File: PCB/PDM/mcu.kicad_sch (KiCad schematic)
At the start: 31 parts, among them IC1 STM32L496ZGT6, IC2 AT25SF128A-SHB-T, Y1 48Mhz, Y2 32KHz

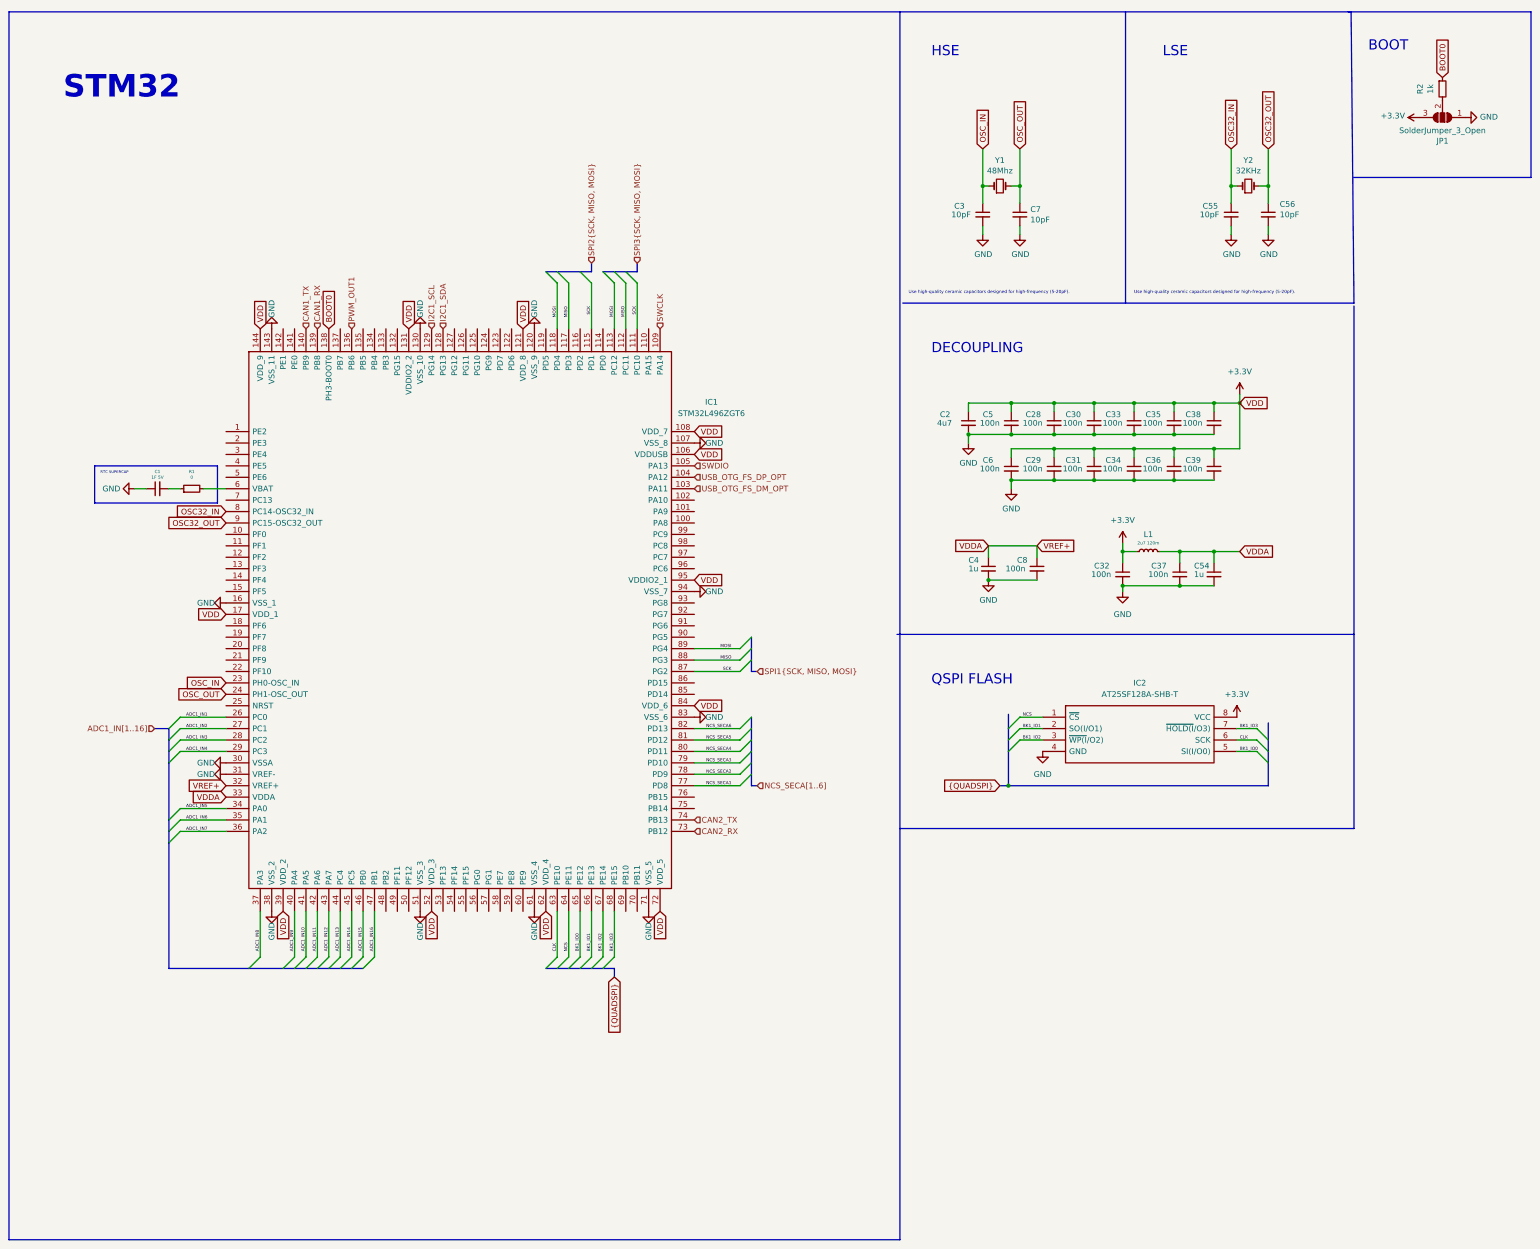
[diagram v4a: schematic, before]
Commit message: Finished high side section & fixed some ERC's errors
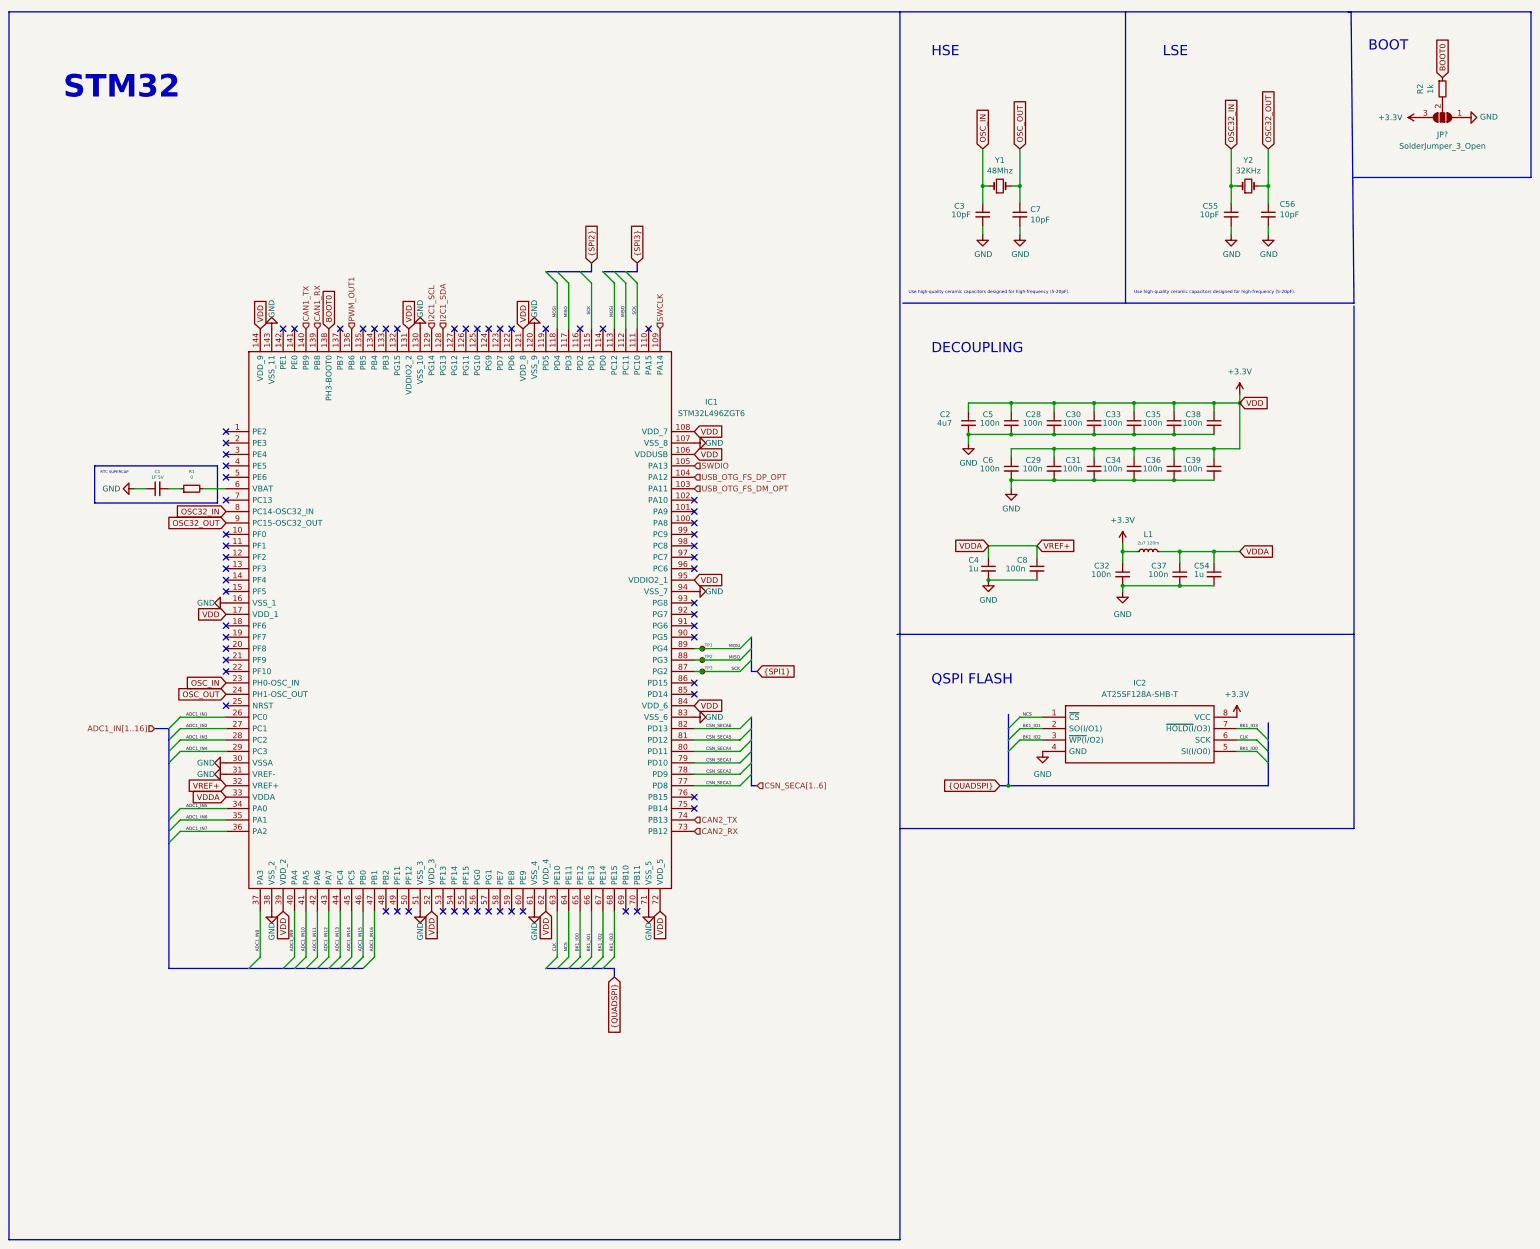
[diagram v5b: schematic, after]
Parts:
- removed JP1: SolderJumper_3_Open, Jumper:SolderJumper-3_P1.3mm_Open_RoundedPad1.0x1.5mm, symbol can2usb-rescue:SolderJumper_3_Open-Jumper
- added JP?: SolderJumper_3_Open, symbol Jumper:SolderJumper_3_Open
- added TP1, TP2, TP3: SPI1_TP, symbol Connector:TestPoint_Small
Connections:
- net +3.3V: now also JP?.3 (B)
- net GND: now also JP?.1 (A)
- net MISO: now also TP2.1
- net MOSI: now also TP1.1
- net SCK: now also TP3.1
- net at R2.2: now also JP?.2 (C)
- net NCS_SECA1 renamed CSN_SECA1
- net NCS_SECA2 renamed CSN_SECA2
- net NCS_SECA3 renamed CSN_SECA3
- net NCS_SECA4 renamed CSN_SECA4
- net NCS_SECA5 renamed CSN_SECA5
- net NCS_SECA6 renamed CSN_SECA6
- no-connect marks 0 -> 63

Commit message: Minor changes in HS sechmatics
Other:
- note added: "ADD adc protection"
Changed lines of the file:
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@@
   (bus_alias "QUADSPI" (members "CLK" "NCS" "BK1_IO0" "BK1_IO1" "BK1_IO2" "BK1_IO3"))
   (bus_alias "SPI1" (members "SCK" "MISO" "MOSI"))
+  (bus_alias "SPI3" (members "SCK" "MISO" "MOSI"))
   (bus_alias "SPI2" (members "SCK" "MISO" "MOSI"))
-  (bus_alias "SPI3" (members "SCK" "MISO" "MOSI"))
   (junction (at 279.4 109.22) (diameter 0) (color 0 0 0 0)
   )
@@
     (stroke (width 0) (type default) (color 0 0 0 0))
   )
-  (polyline (pts (xy 210.185 76.835) (xy 310.515 76.835))
+  (polyline (pts (xy 210.185 76.835) (xy 309.88 76.2))
     (stroke (width 0) (type default) (color 0 0 0 0))
   )
@@
     (stroke (width 0) (type default) (color 0 0 0 0))
   )
-  (polyline (pts (xy 310.515 76.835) (xy 309.88 12.065))
+  (polyline (pts (xy 309.88 76.2) (xy 309.245 11.43))
     (stroke (width 0) (type default) (color 0 0 0 0))
   )
@@
     (stroke (width 0) (type default) (color 0 0 0 0))
   )
-  (polyline (pts (xy 309.88 12.065) (xy 209.55 12.065))
+  (polyline (pts (xy 309.245 11.43) (xy 209.55 12.065))
     (stroke (width 0) (type default) (color 0 0 0 0))
   )
@@
   (text "LSE" (at 267.97 22.225 0)
     (effects (font (size 2.2606 2.2606)) (justify left bottom))
+  )
+  (text "ADD adc protection" (at 21.59 189.23 0)
+    (effects (font (size 1.27 1.27)) (justify left bottom))
   )
   (text "Use high-quality ceramic capacitors designed for high-frequency (5-20pF)."
@@
     (effects (font (size 1.27 1.27)) (justify right))
   )
-  (hierarchical_label "CSN_SECA[1..6]" (shape input) (at 177.8 184.15 0)
+  (hierarchical_label "CSN_SECA[1..8]" (shape input) (at 177.8 184.15 0)
     (effects (font (size 1.27 1.27)) (justify left))
   )
@@
   )
   (symbol (lib_id "PDM_additional:STM32L496ZGT6") (at 59.69 105.41 0) (unit 1)
-    (in_bom yes) (on_board yes) (fields_autoplaced)
-    (property "Reference" "IC1" (id 0) (at 167.64 98.8312 0))
-    (property "Value" "STM32L496ZGT6" (id 1) (at 167.64 101.3712 0))
+    (in_bom yes) (on_board yes)
+    (property "Reference" "IC1" (id 0) (at 113.03 151.13 0))
+    (property "Value" "STM32L496ZGT6" (id 1) (at 113.03 154.94 0))
     (property "Footprint" "PDM_Additional:QFP50P2200X2200X160-144N" (id 2) (at 160.02 87.63 0)
       (effects (font (size 1.27 1.27)) (justify left) hide)

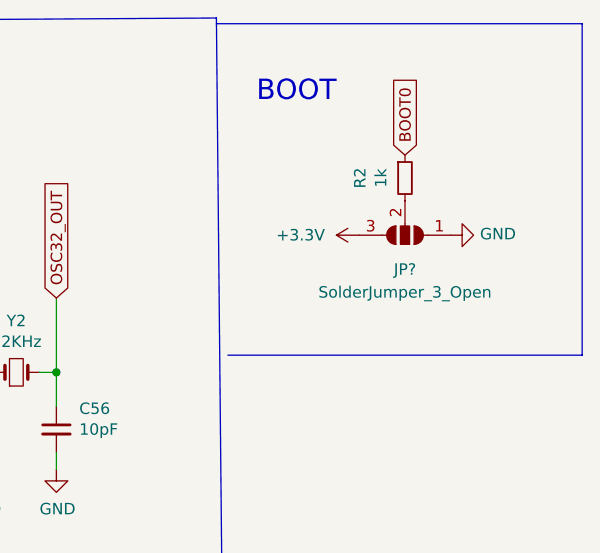
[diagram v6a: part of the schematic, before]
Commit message: Changed MCP2561 to SN65HVD230 for Q1 and 3.3V supply
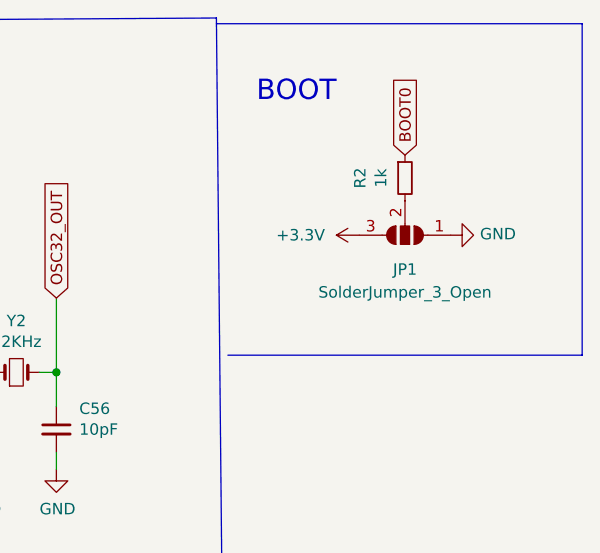
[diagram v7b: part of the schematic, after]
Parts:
- gave numbers to parts that had none: 1
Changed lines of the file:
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@@
   (symbol (lib_id "Jumper:SolderJumper_3_Open") (at 330.2 35.56 180) (unit 1)
     (in_bom yes) (on_board yes) (fields_autoplaced)
-    (property "Reference" "JP?" (id 0) (at 330.2 39.37 0))
+    (property "Reference" "JP1" (id 0) (at 330.2 39.37 0))
     (property "Value" "SolderJumper_3_Open" (id 1) (at 330.2 41.91 0))
     (property "Footprint" "" (id 2) (at 330.2 35.56 0)

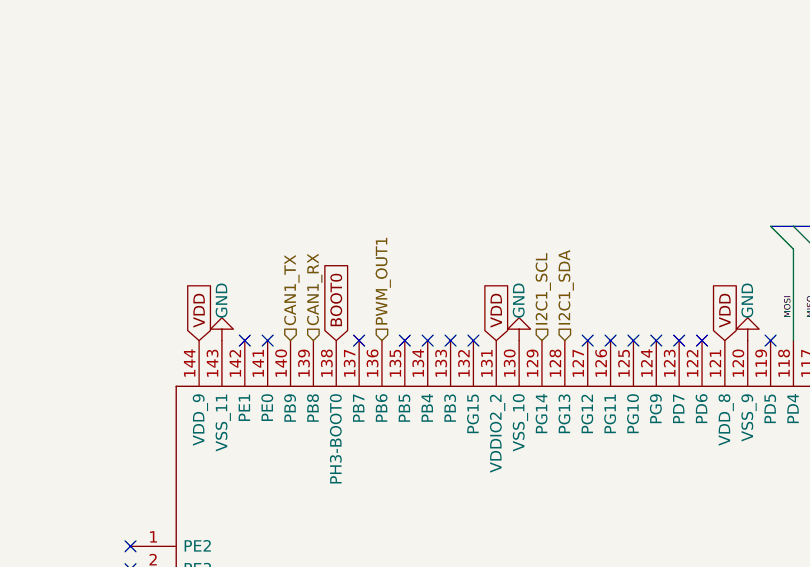
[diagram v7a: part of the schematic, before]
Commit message: Added TE Superseal 1.0 connector 60 pins
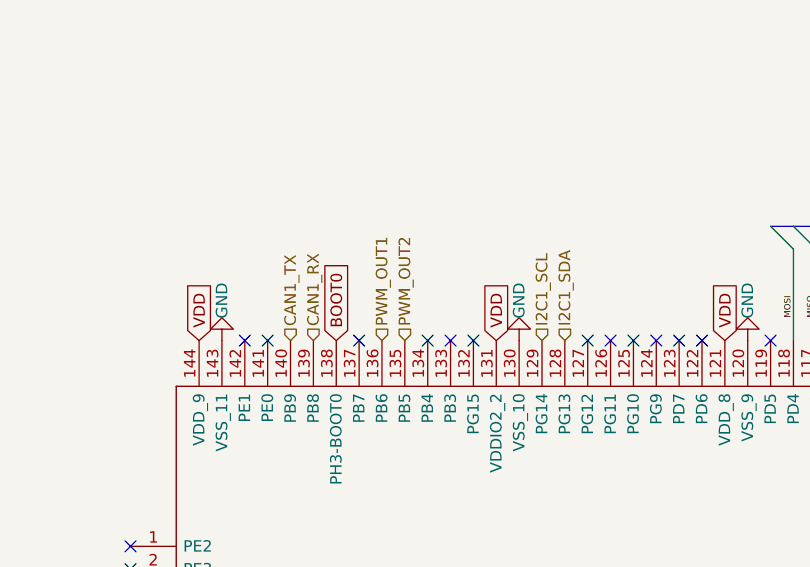
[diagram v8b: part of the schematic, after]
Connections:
- net PWM_OUT2: now reaches IC1.135 (PB5)
- no-connect marks 63 -> 62
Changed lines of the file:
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@@
   (paper "A3")
   (bus_alias "QUADSPI" (members "CLK" "NCS" "BK1_IO0" "BK1_IO1" "BK1_IO2" "BK1_IO3"))
-  (bus_alias "SPI1" (members "SCK" "MISO" "MOSI"))
   (bus_alias "SPI3" (members "SCK" "MISO" "MOSI"))
   (bus_alias "SPI2" (members "SCK" "MISO" "MOSI"))
+  (bus_alias "SPI1" (members "SCK" "MISO" "MOSI"))
   (junction (at 279.4 109.22) (diameter 0) (color 0 0 0 0)
   )
@@
   (no_connect (at 74.93 82.55))
   (no_connect (at 85.09 82.55))
-  (no_connect (at 90.17 82.55))
   (no_connect (at 92.71 82.55))
   (no_connect (at 95.25 82.55))
@@
     (effects (font (size 1.27 1.27)) (justify left))
   )
+  (hierarchical_label "PWM_OUT2" (shape input) (at 90.17 82.55 90)
+    (effects (font (size 1.27 1.27)) (justify left))
+  )
